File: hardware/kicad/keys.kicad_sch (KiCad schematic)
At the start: 21 parts, among them U2001 ME6211C33M5, U2002 MCP3208

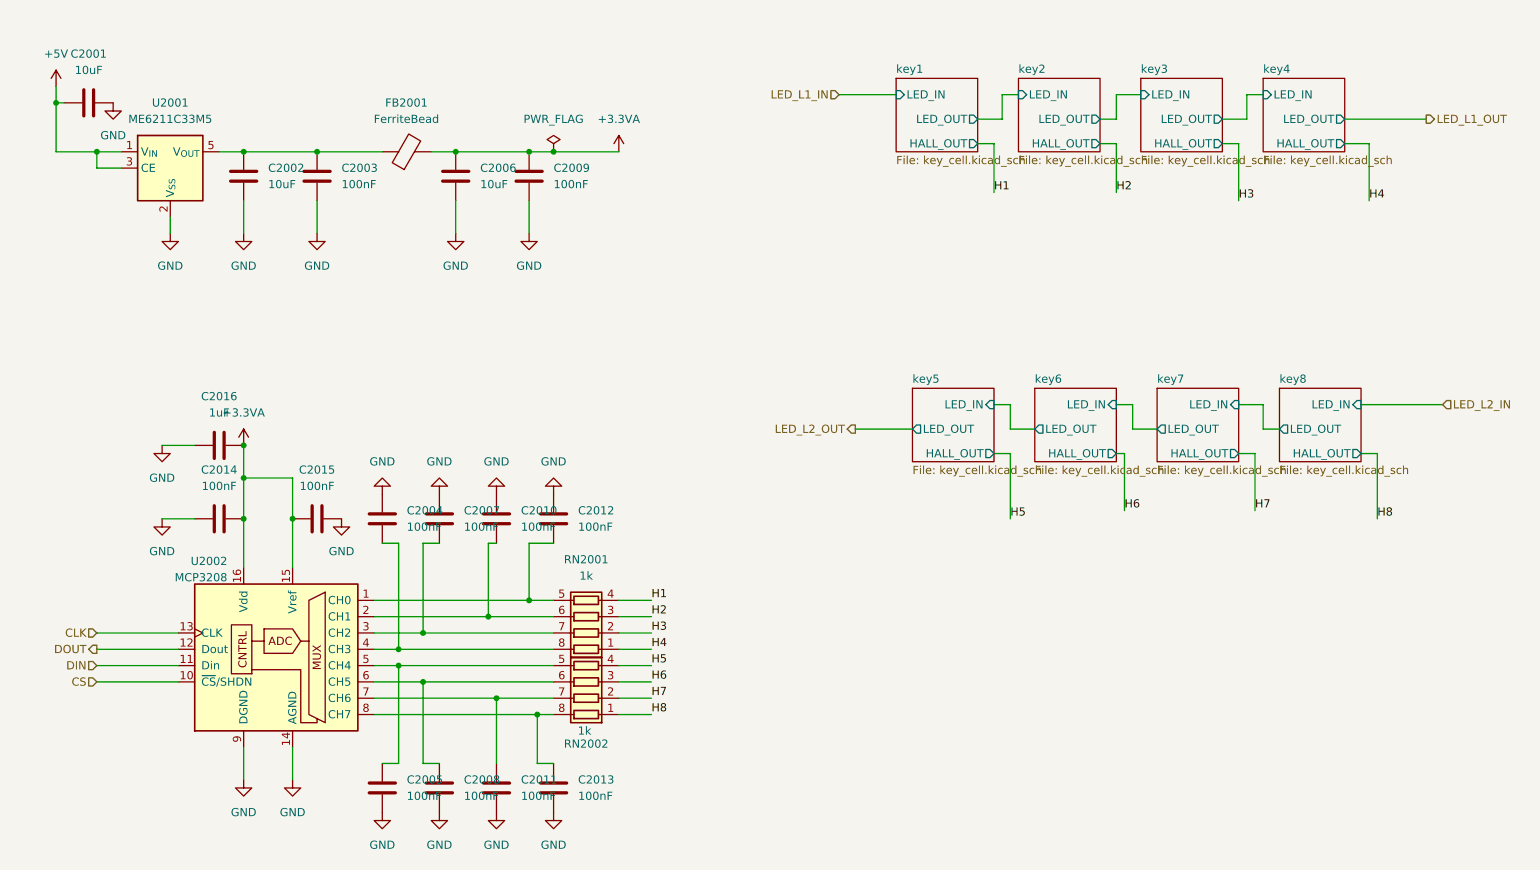
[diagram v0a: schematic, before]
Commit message: WIP checkpoint commit before spliting the 5V rail
hardware/kicad/HALE-H8E10.kicad_pcb: Manufacturing: changed the board
  outline; tenting front back → -; covering - → -; plugging - → -;
  capping - → no; filling - → no; changed the plot output settings.
  Gergő Törcsvári: updated from the schematic (added C1003, C1004,
  C2001-C2016, C3001, C3002, C21001 and 83 more, TP1001-TP1003 not
  placed yet); placed C1003, C1004, C2001-C2016, C3001, C3002, C21001
  and 82 more; routed D_CS, DS_BL, DS_RES, E_INT and 86 more nets; added
  a zone on F.Cu, B.Cu; added a zone on F.Cu, B.Cu; added a zone on
  F.Cu, B.Cu; added a zone on F.Cu, B.Cu; and 15 more changes.
hardware/kicad/HALE-H8E10.kicad_pro: Manufacturing: max arc error - →
  0.005 mm; min connection width - → 0 mm; min groove width - → 0 mm;
  min microvia diameter - → 0.2 mm; min microvia drill - → 0.1 mm; min
  resolved spokes - → 2 mm; solder mask to copper clearance - → 0 mm;
  use height for length calcs - → true mm. Gergő Törcsvári: changed the
  predefined track widths (+4); changed the predefined diff pair sizes
  (+1); changed teardrop settings; changed default text and line
  settings; changed 62 DRC rule severities; changed DRC exclusions;
  changed schematic settings; changed 19 board.design settings settings.
hardware/kicad/HALE-H8E10.kicad_sch: Gergő Törcsvári added R1002, R1003
  and TP1001-TP1003 and wired them; removed C1001, C1002, C1005, D1001
  and D1002; changed C1004 value 100nF → 10uF; changed C1004 footprint
  Capacitor_SMD:C_0603_1608Metric_Pad1.08x0.95mm_HandSolder →
  Capacitor_SMD:C_0805_2012Metric_Pad1.18x1.45mm_HandSolder; changed
  C1004 LCSC C14663 → C15850; changed C1004 wiring (pins 1 and 2 now on
  GND and +5V); changed DS1001 wiring (pin 7 now on /D_CS); and 4 more
  changes.
hardware/kicad/encoders.kicad_sch: Gergő Törcsvári changed U3001 wiring;
  changed U3002 wiring; rearranged the sheet.
hardware/kicad/keys.kicad_sch: Gergő Törcsvári added TP2001 (3V3A) and
  wired it; change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
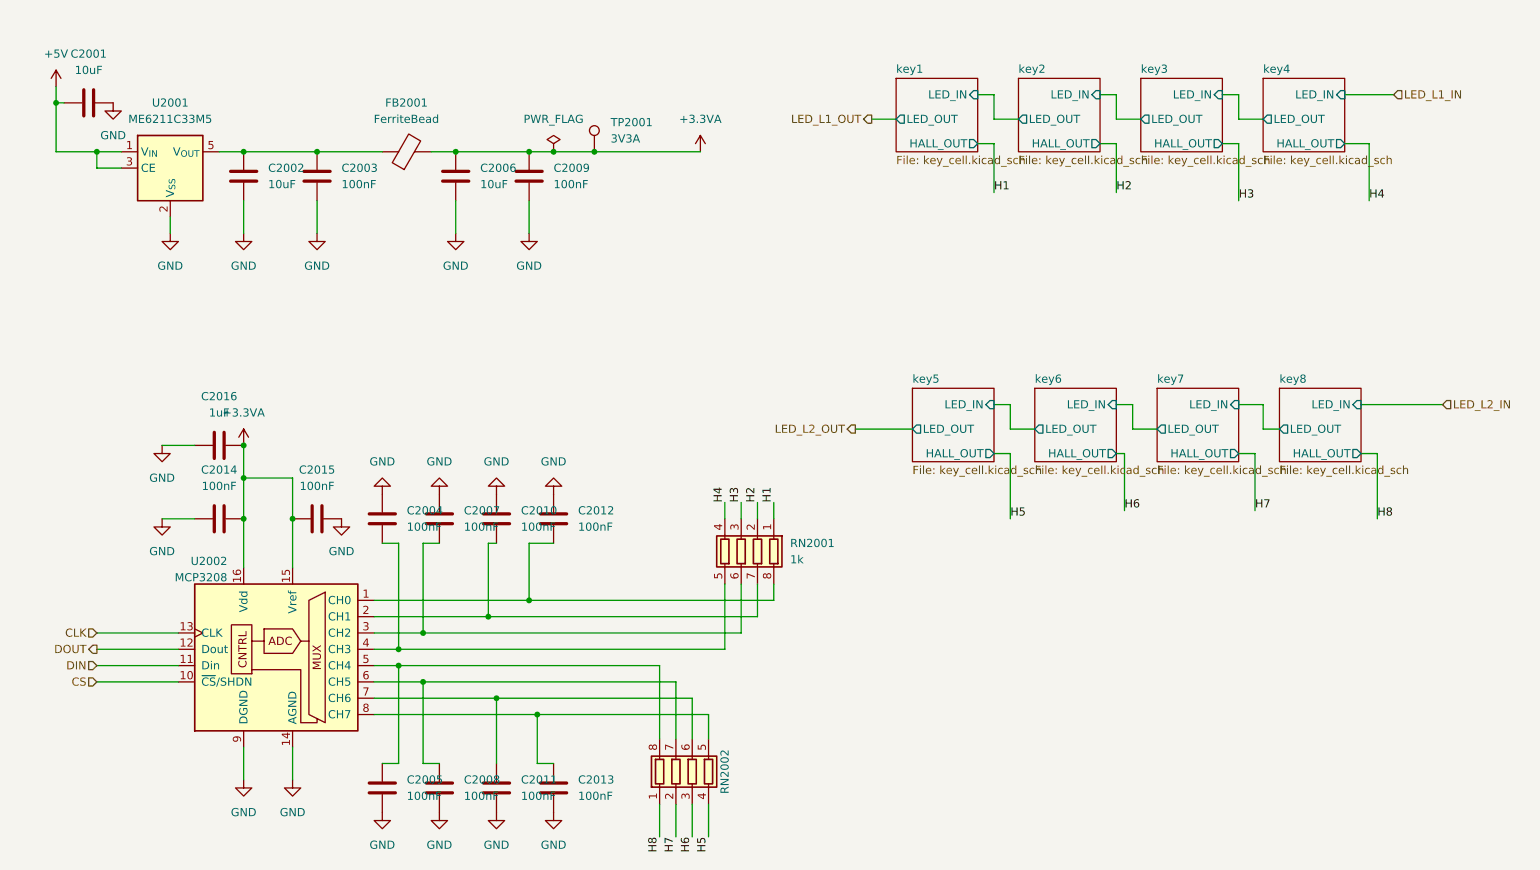
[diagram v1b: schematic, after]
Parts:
- added TP2001: 3V3A, TestPoint:TestPoint_Pad_D2.0mm, symbol Connector:TestPoint
- FB2001: footprint Package_DFN_QFN:Texas_RPU0010A_VQFN-HR-10_2x2mm_P0.5mm -> Inductor_SMD:L_0603_1608Metric_Pad1.05x0.95mm_HandSolder
- RN2001, RN2002: footprint Resistor_THT:R_Array_SIP4 -> Resistor_SMD:R_Array_Convex_4x0603
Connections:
- net +3.3VA: now also TP2001.1
- net H1: now also RN2001.1 (R1.1); no longer RN2001.4 (R4.1)
- net H2: now also RN2001.2 (R2.1); no longer RN2001.3 (R3.1)
- net H3: now also RN2001.3 (R3.1); no longer RN2001.2 (R2.1)
- net H4: now also RN2001.4 (R4.1); no longer RN2001.1 (R1.1)
- net at C2010.1, U2002.2 (CH1): now also RN2001.7 (R2.2); no longer RN2001.6 (R3.2)
- net at C2011.2, U2002.7 (CH6): now also RN2002.6 (R3.2); no longer RN2002.7 (R2.2)
- net at C2012.1, U2002.1 (CH0): now also RN2001.8 (R1.2); no longer RN2001.5 (R4.2)
- net at C2007.1, U2002.3 (CH2): now also RN2001.6 (R3.2); no longer RN2001.7 (R2.2)
- net at C2005.2, U2002.5 (CH4): now also RN2002.8 (R1.2); no longer RN2002.5 (R4.2)
- net at C2004.1, U2002.4 (CH3): now also RN2001.5 (R4.2); no longer RN2001.8 (R1.2)
- net at C2013.2, U2002.8 (CH7): now also RN2002.5 (R4.2); no longer RN2002.8 (R1.2)
- net at C2008.2, U2002.6 (CH5): now also RN2002.7 (R2.2); no longer RN2002.6 (R3.2)
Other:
- moved on the sheet: RN2001, RN2002

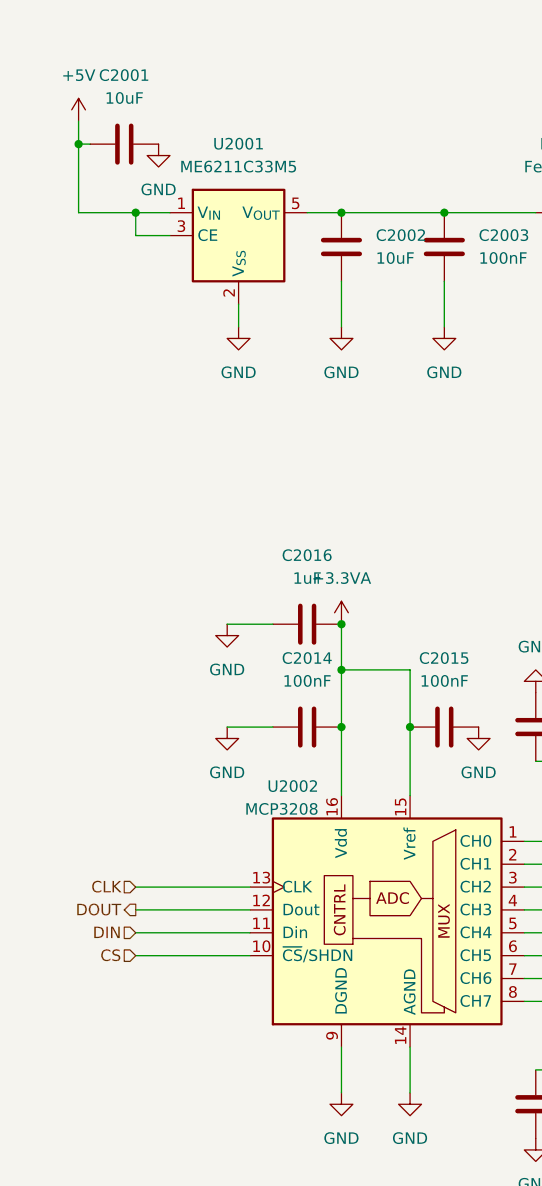
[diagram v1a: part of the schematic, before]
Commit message: "finished" PCB
hardware/kicad/HALE-H8E10.kicad_pcb: Manufacturing: changed the board
  outline. Gergő Törcsvári: updated from the schematic (added C1001,
  C1002, C1004-C1009, H1001-H1012, R1004, R1005 and 5 more; removed
  R1002 and R1003; nets changed on 44 pads); placed C1001, C1002,
  C1004-C1009, H1001-H1012, R1004, R1005 and 4 more; added REF**;
  removed C1004; moved C1003, C2002, C2003, C2006, R1001, TP2001 and
  U1001; routed EN_AUX, EN_LED, +5V_AUX, +5V_LED and 3 more nets;
  rerouted D_CS, DS_BL, DS_RES, E_INT and 21 more nets; and 3 more
  changes.
hardware/kicad/HALE-H8E10.kicad_pro: Gergő Törcsvári excluded 2 DRC
  violations; changed schematic settings.
hardware/kicad/HALE-H8E10.kicad_sch: Gergő Törcsvári added C1001, C1002,
  C1005-C1009, H1001-H1012, R1004, R1005 and 4 more and wired them;
  removed R1002 and R1003; changed 4 parts' fields; changed C1004 wiring
  (pin 1 now on +5V); renamed net unconnected-(U1002-D3-Pad4) to
  /EN_AUX; renamed net unconnected-(U1002-D15-Pad19) to /EN_LED; split
  +5V into +5V_AUX and +5V_LED; and 4 more changes.
hardware/kicad/encoder.kicad_sch: Gergő Törcsvári changed 10 parts'
  fields; renamed net unconnected-(U1002-D3-Pad4) to /EN_AUX; renamed
  net unconnected-(U1002-D15-Pad19) to /EN_LED; split +5V into +5V_AUX
  and +5V_LED.
hardware/kicad/encoders.kicad_sch: Gergő Törcsvári changed 6 parts'
  fields; renamed net unconnected-(U1002-D3-Pad4) to /EN_AUX; renamed
  net unconnected-(U1002-D15-Pad19) to /EN_LED; split +5V into +5V_AUX
  and +5V_LED.
hardware/kicad/key_cell.kicad_sch: Gergő Törcsvári changed 16 parts'
  fields; renamed net unconnected-(U1002-D3-Pad4) to /EN_AUX; renamed
  net unconnected-(U1002-D15-Pad19) to /EN_LED; split +5V into +5V_AUX
  and +5V_LED.
hardware/kicad/keys.kicad_sch: Gergő Törcsvári added R2001 (10K) and
  wired it to /KEYS_CS; changed 6 parts' fields; renamed net
  unconnected-(U1002-D3-Pad4) to /EN_AUX; renamed net
  unconnected-(U1002-D15-Pad19) to /EN_LED; split +5V into +5V_A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
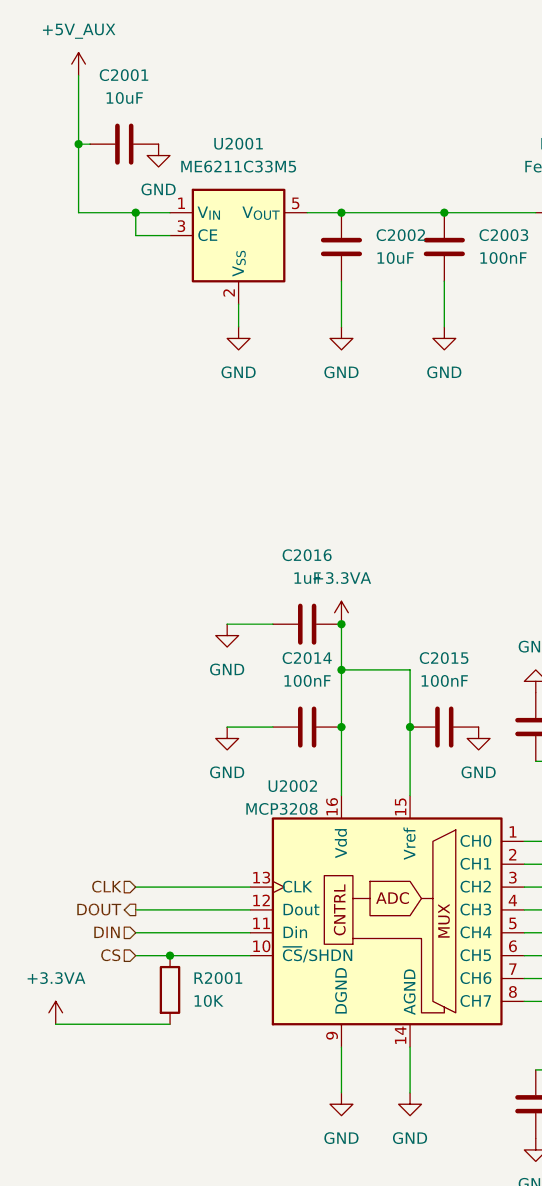
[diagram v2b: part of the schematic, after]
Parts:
- added R2001: 10K, Resistor_SMD:R_0603_1608Metric_Pad0.98x0.95mm_HandSolder, symbol Device:R
- C2016: LCSC C14663 -> C15849
- FB2001: LCSC (none) -> C1002
- RN2001, RN2002: LCSC (none) -> C20197
- U2001: LCSC (none) -> C82942
- U2002: LCSC (none) -> C626764
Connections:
- net +3.3VA: now also R2001.2
- net CS: now also R2001.1
- net +5V renamed +5V_AUX
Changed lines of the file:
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@@
 			)
 		)
-		(property "LCSC" ""
+		(property "LCSC" "C1002"
 			(at 74.93 36.83 90)
 			(hide yes)
@@
 		)
 	)
-	(symbol
-		(lib_id "power:+5V")
-		(at 20.32 26.67 0)
-		(unit 1)
-		(body_style 1)
-		(exclude_from_sim no)
-		(in_bom yes)
-		(on_board yes)
-		(in_pos_files yes)
-		(dnp no)
-		(fields_autoplaced yes)
-		(property "Reference" "#PWR02001"
-			(at 20.32 30.48 0)
-			(hide yes)
-			(show_name no)
-			(do_not_autoplace no)
-			(effects
-				(font
-					(size 1.27 1.27)
-				)
-			)
-		)
-		(property "Value" "+5V"
-			(at 20.32 21.59 0)
-			(show_name no)
-			(do_not_autoplace no)
-			(effects
-				(font
-					(size 1.27 1.27)
-				)
-			)
-		)
-		(property "Footprint" ""
-			(at 20.32 26.67 0)
-			(hide yes)
-			(show_name no)
-			(do_not_autoplace no)
-			(effects
-				(font
-					(size 1.27 1.27)
-				)
-			)
-		)
-		(property "Datasheet" ""
-			(at 20.32 26.67 0)
-			(hide yes)
-			(show_name no)
-			(do_not_autoplace no)
-			(effects
-				(font
-					(size 1.27 1.27)
-				)
-			)
-		)
-		(property "Description" "Power symbol creates a global label with name \"+5V\""
-			(at 20.32 26.67 0)
-			(hide yes)
-			(show_name no)
-			(do_not_autoplace no)
-			(effects
-				(font
-					(size 1.27 1.27)
-				)
-			)
-		)
-		(pin "1"
-		)
-		(instances
-			(project "HALE-H8E10"
-				(path "/95d89127-9479-4179-8532-6fc4e4c352d8/4b75bd9e-329e-4489-b23d-ebc8bc921298"
-					(reference "#PWR02001")
-					(unit 1)
-				)
-			)
-		)
-	)
 	(junction
 		(at 82.55 36.83)
@@
 			)
 		)
-		(property "LCSC" ""
+		(property "LCSC" "C82942"
 			(at 38.1 39.37 0)
 			(hide yes)
@@
 			)
 		)
-		(property "LCSC" ""
+		(property "LCSC" "C626764"
 			(at 54.61 114.3 0)
 			(hide yes)
@@
 	(wire
 		(pts
-			(xy 20.32 26.67) (xy 20.32 29.21)
+			(xy 20.32 21.59) (xy 20.32 29.21)
 		)
 		(stroke
@@
 			)
 		)
-		(property "LCSC" ""
+		(property "LCSC" "C20197"
 			(at 127 99.06 90)
 			(hide yes)
@@
 			)
 		)
-		(property "LCSC" ""
+		(property "LCSC" "C20197"
 			(at 119.38 133.35 90)
 			(hide yes)
@@
 	(wire
 		(pts
-			(xy 26.67 119.38) (xy 39.37 119.38)
+			(xy 26.67 119.38) (xy 30.48 119.38)
 		)
 		(stroke
@@
 			)
 		)
-		(property "LCSC" "C14663"
+		(property "LCSC" "C15849"
 			(at 45.72 82.55 0)
 			(hide yes)
@@
 		)
 		(stroke
+			(width 0)
+			(type default)
+		)
+	)
+	(symbol
+		(lib_id "power:+5VL")
+		(at 20.32 21.59 0)
+		(unit 1)
+		(body_style 1)
+		(exclude_from_sim no)
+		(in_bom yes)
+		(on_board yes)
+		(in_pos_files yes)
+		(dnp no)
+		(fields_autoplaced yes)
+		(property "Reference" "#PWR02001"
+			(at 20.32 25.4 0)
+			(hide yes)
+			(show_name no)
+			(do_not_autoplace no)
+			(effects
+				(font
+					(size 1.27 1.27)
+				)
+			)
+		)
+		(property "Value" "+5V_AUX"
+			(at 20.32 16.51 0)
+			(show_name no)
+			(do_not_autoplace no)
+			(effects
+				(font
+					(size 1.27 1.27)
+				)
+			)
+		)
+		(property "Footprint" ""
+			(at 20.32 21.59 0)
+			(hide yes)
+			(show_name no)
+			(do_not_autoplace no)
+			(effects
+				(font
+					(size 1.27 1.27)
+				)
+			)
+		)
+		(property "Datasheet" ""
+			(at 20.32 21.59 0)
+			(hide yes)
+			(show_name no)
+			(do_not_autoplace no)
+			(effects
+				(font
+					(size 1.27 1.27)
+				)
+			)
+		)
+		(property "Description" "Power symbol creates a global label with name \"+5VL\""
+			(at 20.32 21.59 0)
+			(hide yes)
+			(show_name no)
+			(do_not_autoplace no)
+			(effects
+				(font
+					(size 1.27 1.27)
+				)
+			)
+		)
+		(pin "1"
+		)
+		(instances
+			(project "HALE-H8E10"
+				(path "/95d89127-9479-4179-8532-6fc4e4c352d8/4b75bd9e-329e-4489-b23d-ebc8bc921298"
+					(reference "#PWR02001")
+					(unit 1)
+				)
+			)
+		)
+	)
+	(junction
+		(at 30.48 119.38)
+		(diameter 0)
+		(color 0 0 0 0)
+	)
+	(wire
+		(pts
+			(xy 30.48 119.38) (xy 39.37 119.38)
+		)
+		(stroke
+			(width 0)
+			(type default)
+		)
+	)
+	(symbol
+		(lib_id "Device:R")
+		(at 30.48 123.19 0)
+		(unit 1)
+		(body_style 1)
+		(exclude_from_sim no)
+		(in_bom yes)
+		(on_board yes)
+		(in_pos_files yes)
+		(dnp no)
+		(fields_autoplaced yes)
+		(property "Reference" "R2001"
+			(at 33.02 121.9199 0)
+			(show_name no)
+			(do_not_autoplace no)
+			(effects
+				(font
+					(size 1.27 1.27)
+				)
+				(justify left)
+			)
+		)
+		(property "Value" "10K"
+			(at 33.02 124.4599 0)
+			(show_name no)
+			(do_not_autoplace no)
+			(effects
+				(font
+					(size 1.27 1.27)
+				)
+				(justify left)
+			)
+		)
+		(property "Footprint" "Resistor_SMD:R_0603_1608Metric_Pad0.98x0.95mm_HandSolder"
+			(at 28.702 123.19 90)
+			(hide yes)
+			(show_name no)
+			(do_not_autoplace no)
+			(effects
+				(font
+					(size 1.27 1.27)
+				)
+			)
+		)
+		(property "Datasheet" ""
+			(at 30.48 123.19 0)
+			(hide yes)
+			(show_name no)
+			(do_not_autoplace no)
+			(effects
+				(font
+					(size 1.27 1.27)
+				)
+			)
+		)
+		(property "Description" "Resistor"
+			(at 30.48 123.19 0)
+			(hide yes)
+			(show_name no)
+			(do_not_autoplace no)
+			(effects
+				(font
+					(size 1.27 1.27)
+				)
+			)
+		)
+		(property "LCSC" "C25804"
+			(at 30.48 123.19 90)
+			(hide yes)
+			(show_name no)
+			(do_not_autoplace no)
+			(effects
+				(font
+					(size 1.27 1.27)
+				)
+			)
+		)
+		(pin "2"
+		)
+		(pin "1"
+		)
+		(instances
+			(project "HALE-H8E10"
+				(path "/95d89127-9479-4179-8532-6fc4e4c352d8/4b75bd9e-329e-4489-b23d-ebc8bc921298"
+					(reference "R2001")
+					(unit 1)
+				)
+			)
+		)
+	)
+	(symbol
+		(lib_id "power:+3.3VA")
+		(at 17.78 127 0)
+		(unit 1)
+		(body_style 1)
+		(exclude_from_sim no)
+		(in_bom yes)
+		(on_board yes)
+		(in_pos_files yes)
+		(dnp no)
+		(fields_autoplaced yes)
+		(property "Reference" "#PWR02023"
+			(at 17.78 130.81 0)
+			(hide yes)
+			(show_name no)
+			(do_not_autoplace no)
+			(effects
+				(font
+					(size 1.27 1.27)
+				)
+			)
+		)
+		(property "Value" "+3.3VA"
+			(at 17.78 121.92 0)
+			(show_name no)
+			(do_not_autoplace no)
+			(effects
+				(font
+					(size 1.27 1.27)
+				)
+			)
+		)
+		(property "Footprint" ""
+			(at 17.78 127 0)
+			(hide yes)
+			(show_name no)
+			(do_not_autoplace no)
+			(effects
+				(font
+					(size 1.27 1.27)
+				)
+			)
+		)
+		(property "Datasheet" ""
+			(at 17.78 127 0)
+			(hide yes)
+			(show_name no)
+			(do_not_autoplace no)
+			(effects
+				(font
+					(size 1.27 1.27)
+				)
+			)
+		)
+		(property "Description" "Power symbol creates a global label with name \"+3.3VA\""
+			(at 17.78 127 0)
+			(hide yes)
+			(show_name no)
+			(do_not_autoplace no)
+			(effects
+				(font
+					(size 1.27 1.27)
+				)
+			)
+		)
+		(pin "1"
+		)
+		(instances
+			(project "HALE-H8E10"
+				(path "/95d89127-9479-4179-8532-6fc4e4c352d8/4b75bd9e-329e-4489-b23d-ebc8bc921298"
+					(reference "#PWR02023")
+					(unit 1)
+				)
+			)
+		)
+	)
+	(wire
+		(pts
+			(xy 17.78 127) (xy 30.48 127)
+		)
+		(stroke
